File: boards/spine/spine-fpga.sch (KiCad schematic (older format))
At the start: 24 parts, among them U7 iCE40-HX1K-TQ144

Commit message: Schematic footprint and refdes work
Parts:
- U7: footprint (none) -> Housings_QFP:TQFP-144_20x20mm_Pitch0.5mm
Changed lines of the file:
@@
 F 0 "U7" H 2750 1800 60  0000 L CNN
 F 1 "iCE40-HX1K-TQ144" H 2750 1700 60  0000 L CNN
-F 2 "" H 2550 1550 60  0001 C CNN
+F 2 "Housings_QFP:TQFP-144_20x20mm_Pitch0.5mm" H 2550 1550 60  0001 C CNN
 F 3 "http://www.latticesemi.com/~/media/LatticeSemi/Documents/DataSheets/iCE/iCE40LPHXFamilyDataSheet.pdf" H 2550 1550 60  0001 C CNN
 F 4 "4.5703" H 2550 1550 60  0001 C CNN "RefPrice1k"
@@
 F 0 "U7" H 5850 1150 60  0000 L CNN
 F 1 "iCE40-HX1K-TQ144" H 5850 1050 60  0000 L CNN
-F 2 "" H 5650 900 60  0001 C CNN
+F 2 "Housings_QFP:TQFP-144_20x20mm_Pitch0.5mm" H 5650 900 60  0001 C CNN
 F 3 "" H 5650 900 60  0000 C CNN
 	2    5650 900
@@
 F 0 "U7" H 8450 1150 60  0000 L CNN
 F 1 "iCE40-HX1K-TQ144" H 8450 1050 60  0000 L CNN
-F 2 "" H 8250 900 60  0001 C CNN
+F 2 "Housings_QFP:TQFP-144_20x20mm_Pitch0.5mm" H 8250 900 60  0001 C CNN
 F 3 "" H 8250 900 60  0000 C CNN
 	3    8250 900
@@
 F 0 "U7" H 8450 4500 60  0000 L CNN
 F 1 "iCE40-HX1K-TQ144" H 8450 4400 60  0000 L CNN
-F 2 "" H 8250 4250 60  0001 C CNN
+F 2 "Housings_QFP:TQFP-144_20x20mm_Pitch0.5mm" H 8250 4250 60  0001 C CNN
 F 3 "" H 8250 4250 60  0000 C CNN
 	4    8250 4250
@@
 F 0 "U7" H 5850 4300 60  0000 L CNN
 F 1 "iCE40-HX1K-TQ144" H 5850 4200 60  0000 L CNN
-F 2 "" H 5650 4050 60  0001 C CNN
+F 2 "Housings_QFP:TQFP-144_20x20mm_Pitch0.5mm" H 5650 4050 60  0001 C CNN
 F 3 "" H 5650 4050 60  0000 C CNN
 	5    5650 4050
@@
 F 0 "U7" H 2650 3850 60  0000 L CNN
 F 1 "iCE40-HX1K-TQ144" H 2650 3750 60  0000 L CNN
-F 2 "" H 2450 3600 60  0001 C CNN
+F 2 "Housings_QFP:TQFP-144_20x20mm_Pitch0.5mm" H 2450 3600 60  0001 C CNN
 F 3 "" H 2450 3600 60  0000 C CNN
 	6    2450 3600
@@
 $EndComp
 $Comp
-L GND #PWR0106
+L GND #PWR113
 U 1 1 56403C36
 P 2550 1550
-F 0 "#PWR0106" H 2550 1300 50  0001 C CNN
+F 0 "#PWR113" H 2550 1300 50  0001 C CNN
 F 1 "GND" V 2550 1350 50  0000 C CNN
 F 2 "" H 2550 1550 60  0000 C CNN
@@
 $EndComp
 $Comp
-L +1V2 #PWR0107
+L +1V2 #PWR114
 U 1 1 564083AC
 P 2550 1850
-F 0 "#PWR0107" H 2550 1700 50  0001 C CNN
+F 0 "#PWR114" H 2550 1700 50  0001 C CNN
 F 1 "+1V2" V 2550 2050 50  0000 C CNN
 F 2 "" H 2550 1850 60  0000 C CNN
@@
 	1600 1250 1600 1950
 $Comp
-L +1V2 #PWR0108
+L +1V2 #PWR110
 U 1 1 5640879A
 P 1600 950
-F 0 "#PWR0108" H 1600 800 50  0001 C CNN
+F 0 "#PWR110" H 1600 800 50  0001 C CNN
 F 1 "+1V2" H 1600 1100 50  0000 C CNN
 F 2 "" H 1600 950 60  0000 C CNN
@@
 NoConn ~ 2550 2150
 $Comp
-L +3V3 #PWR0109
+L +3V3 #PWR119
 U 1 1 5640CF73
 P 5650 6450
-F 0 "#PWR0109" H 5650 6300 50  0001 C CNN
+F 0 "#PWR119" H 5650 6300 50  0001 C CNN
 F 1 "+3V3" V 5650 6700 50  0000 C CNN
 F 2 "" H 5650 6450 60  0000 C CNN
@@
 SPI_SS
 $Comp
-L +3V3 #PWR0110
+L +3V3 #PWR111
 U 1 1 5640D6CD
 P 2100 2900
-F 0 "#PWR0110" H 2100 2750 50  0001 C CNN
+F 0 "#PWR111" H 2100 2750 50  0001 C CNN
 F 1 "+3V3" H 2100 3040 50  0000 C CNN
 F 2 "" H 2100 2900 60  0000 C CNN
@@
 Connection ~ 2100 3050
 $Comp
-L GND #PWR0111
+L GND #PWR112
 U 1 1 5640DE11
 P 2100 4500
-F 0 "#PWR0111" H 2100 4250 50  0001 C CNN
+F 0 "#PWR112" H 2100 4250 50  0001 C CNN
 F 1 "GND" H 2100 4350 50  0000 C CNN
 F 2 "" H 2100 4500 60  0000 C CNN
@@
 $EndComp
 $Comp
-L +3V3 #PWR0112
+L +3V3 #PWR118
 U 1 1 5640E61C
 P 5650 3200
-F 0 "#PWR0112" H 5650 3050 50  0001 C CNN
+F 0 "#PWR118" H 5650 3050 50  0001 C CNN
 F 1 "+3V3" V 5650 3450 50  0000 C CNN
 F 2 "" H 5650 3200 60  0000 C CNN
@@
 $EndComp
 $Comp
-L +3V3 #PWR0113
+L +3V3 #PWR121
 U 1 1 5640E78F
 P 8250 3400
-F 0 "#PWR0113" H 8250 3250 50  0001 C CNN
+F 0 "#PWR121" H 8250 3250 50  0001 C CNN
 F 1 "+3V3" V 8250 3650 50  0000 C CNN
 F 2 "" H 8250 3400 60  0000 C CNN
@@
 $EndComp
 $Comp
-L +3V3 #PWR0114
+L +3V3 #PWR122
 U 1 1 5640E7E2
 P 8250 6450
-F 0 "#PWR0114" H 8250 6300 50  0001 C CNN
+F 0 "#PWR122" H 8250 6300 50  0001 C CNN
 F 1 "+3V3" V 8250 6700 50  0000 C CNN
 F 2 "" H 8250 6450 60  0000 C CNN
@@
 $EndComp
 $Comp
-L +1V2 #PWR0115
+L +1V2 #PWR106
 U 1 1 5640EE64
 P 1450 5250
-F 0 "#PWR0115" H 1450 5100 50  0001 C CNN
+F 0 "#PWR106" H 1450 5100 50  0001 C CNN
 F 1 "+1V2" H 1450 5400 50  0000 C CNN
 F 2 "" H 1450 5250 60  0000 C CNN
@@
 $EndComp
 $Comp
-L +3V3 #PWR0116
+L +3V3 #PWR108
 U 1 1 5640F3E2
 P 1450 6500
-F 0 "#PWR0116" H 1450 6350 50  0001 C CNN
+F 0 "#PWR108" H 1450 6350 50  0001 C CNN
 F 1 "+3V3" H 1450 6640 50  0000 C CNN
 F 2 "" H 1450 6500 60  0000 C CNN
@@
 Connection ~ 4250 7100
 $Comp
-L GND #PWR0117
+L GND #PWR107
 U 1 1 5640FDCB
 P 1450 5950
-F 0 "#PWR0117" H 1450 5700 50  0001 C CNN
+F 0 "#PWR107" H 1450 5700 50  0001 C CNN
 F 1 "GND" H 1450 5800 50  0000 C CNN
 F 2 "" H 1450 5950 60  0000 C CNN
@@
 $EndComp
 $Comp
-L GND #PWR0118
+L GND #PWR109
 U 1 1 5640FE24
 P 1450 7200
-F 0 "#PWR0118" H 1450 6950 50  0001 C CNN
+F 0 "#PWR109" H 1450 6950 50  0001 C CNN
 F 1 "GND" H 1450 7050 50  0000 C CNN
 F 2 "" H 1450 7200 60  0000 C CNN
@@
 Connection ~ 7950 4350
 $Comp
-L +3V3 #PWR0119
+L +3V3 #PWR120
 U 1 1 56410A99
 P 7750 3750
-F 0 "#PWR0119" H 7750 3600 50  0001 C CNN
+F 0 "#PWR120" H 7750 3600 50  0001 C CNN
 F 1 "+3V3" H 7750 3890 50  0000 C CNN
 F 2 "" H 7750 3750 60  0000 C CNN
@@
 Connection ~ 2150 1650
 $Comp
-L +2V5 #PWR0120
+L +2V5 #PWR115
 U 1 1 5644292C
 P 2550 2050
-F 0 "#PWR0120" H 2550 1900 50  0001 C CNN
+F 0 "#PWR115" H 2550 1900 50  0001 C CNN
 F 1 "+2V5" V 2550 2250 50  0000 C CNN
 F 2 "" H 2550 2050 60  0000 C CNN
@@
 	3400 5750 3400 5950
 $Comp
-L GND #PWR0121
+L GND #PWR117
 U 1 1 56443449
 P 3400 5950
-F 0 "#PWR0121" H 3400 5700 50  0001 C CNN
+F 0 "#PWR117" H 3400 5700 50  0001 C CNN
 F 1 "GND" H 3400 5800 50  0000 C CNN
 F 2 "" H 3400 5950 60  0000 C CNN
@@
 $EndComp
 $Comp
-L +2V5 #PWR0122
+L +2V5 #PWR116
 U 1 1 56443529
 P 3400 5250
-F 0 "#PWR0122" H 3400 5100 50  0001 C CNN
+F 0 "#PWR116" H 3400 5100 50  0001 C CNN
 F 1 "+2V5" H 3400 5390 50  0000 C CNN
 F 2 "" H 3400 5250 60  0000 C CNN
@@
 72 0F 1C A9 DC 70 49 CB 79 33 88 85 99 AD 01 6C 4B 10 FC 3B 13 DE 3B 37 68 79 AD 07 BC 00 3C 0E
 3C 31 EE E3 D8 E7 0F 03 D7 7B 9F FB C1 E1 FF 01 18 C4 96 1D B8 0E 40 07 00 00 00 00 49 45 4E 44
-AE 42 60 82 CA
+AE 42 60 82 00
 EndData
 $EndBitmap

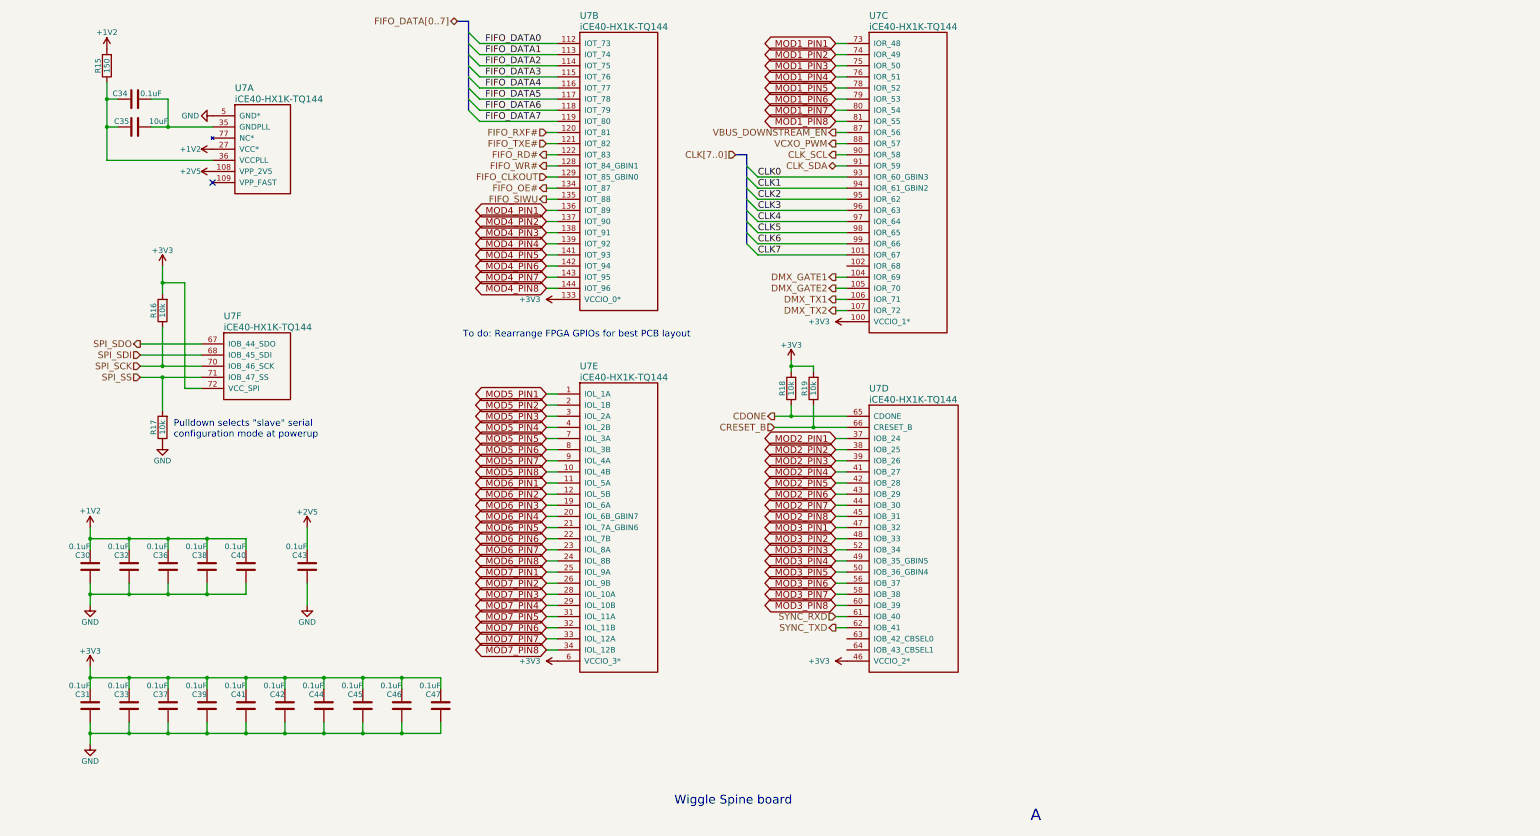
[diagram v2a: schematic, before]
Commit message: Simpler indicator LED strategy
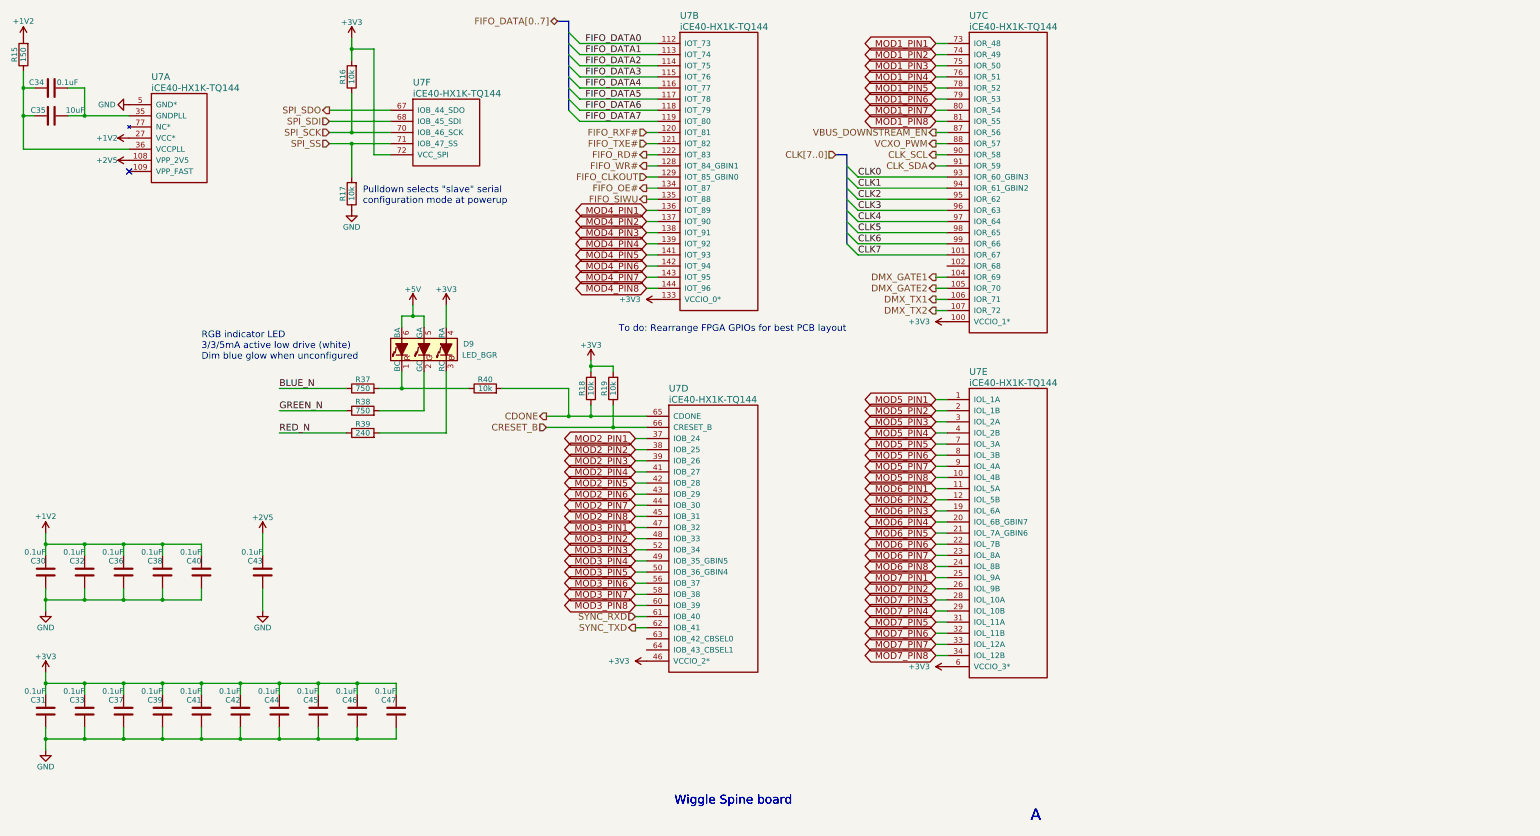
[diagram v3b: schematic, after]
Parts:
- added D9: LED_BGR, LEDs:LED_RGB_PLLC-6, symbol LED_BGR
- added R37, R38: 750, Resistors_SMD:R_0805, symbol R
- added R39: 240, Resistors_SMD:R_0805, symbol R
- added R40: 10k, Resistors_SMD:R_0805, symbol R
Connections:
- net +3V3: now also D9.4 (RA)
- net CDONE: now also R40.2
- new net: D9.1 (BC), R37.2, R40.1
- new net: D9.2 (GC), R38.2
- new net: D9.3 (RC), R39.2
- new net +5V: D9.5 (GA), D9.6 (BA)
- new net BLUE_N: R37.1
- new net GREEN_N: R38.1
- new net RED_N: R39.1
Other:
- note added: "RGB indicator LED\n3/3/5mA active low drive (white)\nDim blue glow when unconfigured"
- moved on the sheet: C30, C31, C32, C33, C34, C35, C36, C37, C38, C39, C40, C41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

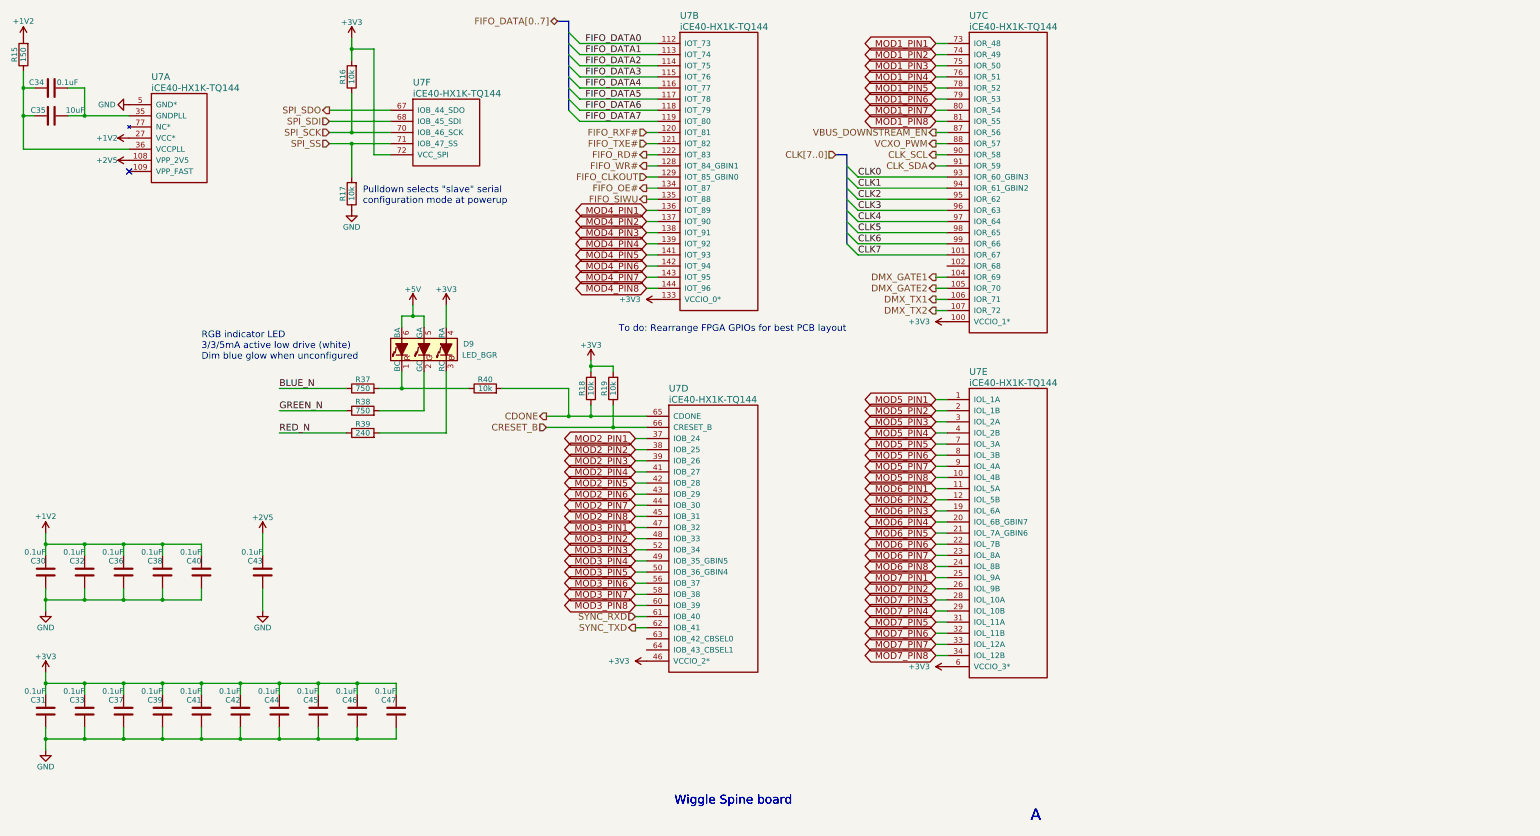
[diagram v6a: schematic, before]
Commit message: Order and routing for FIFO parallel bus
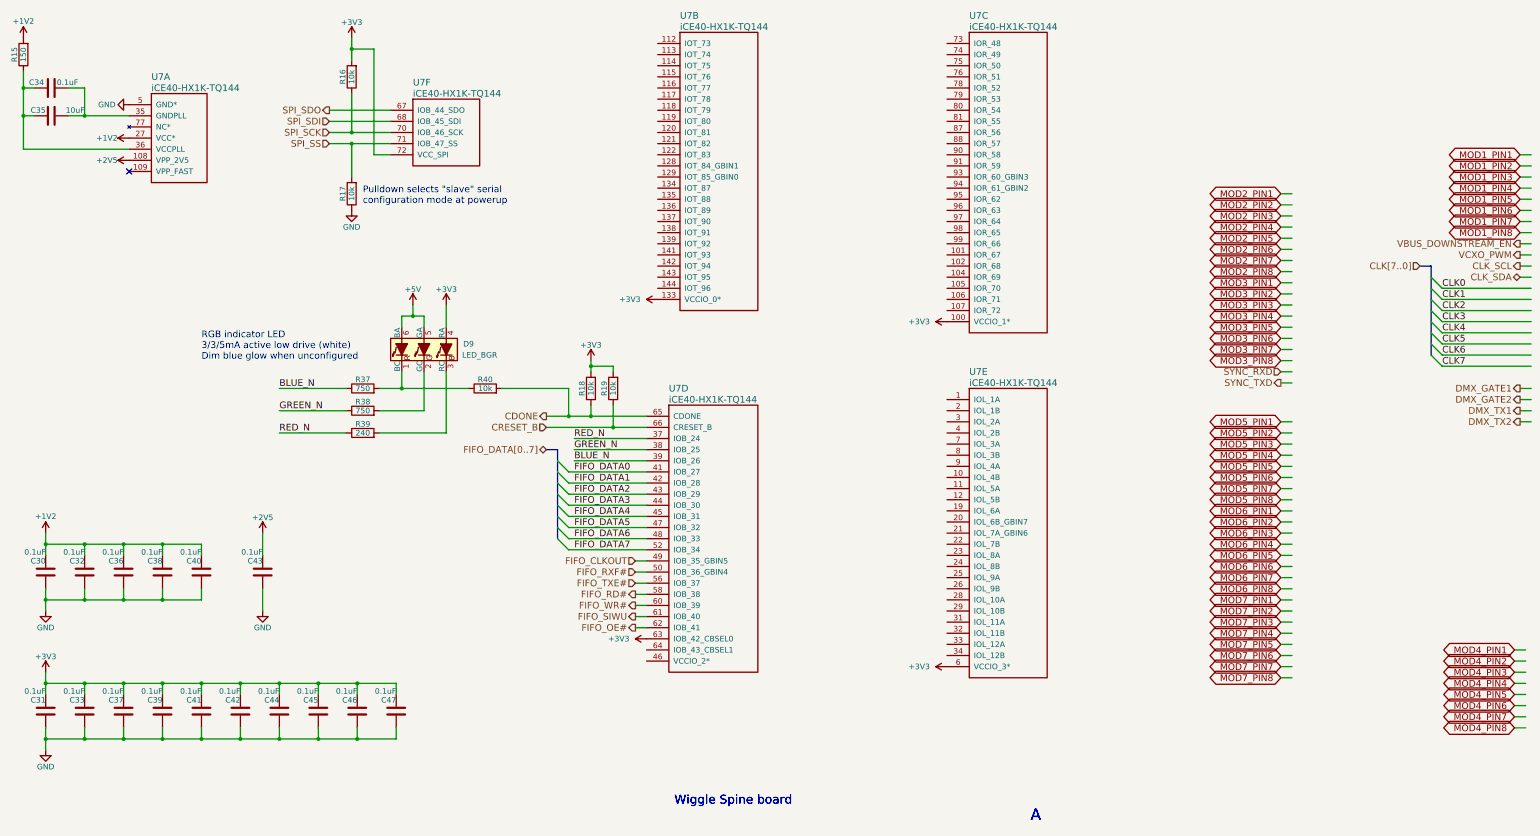
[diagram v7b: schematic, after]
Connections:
- wire segments 165 -> 168
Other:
- note removed: "To do: Rearrange FPGA GPIOs for best PCB layout"
